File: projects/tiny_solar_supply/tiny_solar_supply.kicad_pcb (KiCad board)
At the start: 2 copper layers, 16 parts, among them J1 Conn_01x02, J2 Conn_01x02, J3 Conn_01x02, J4 Conn_01x02, T1 2N7002 (SOT-23), U1 AP3015AKTR-G1

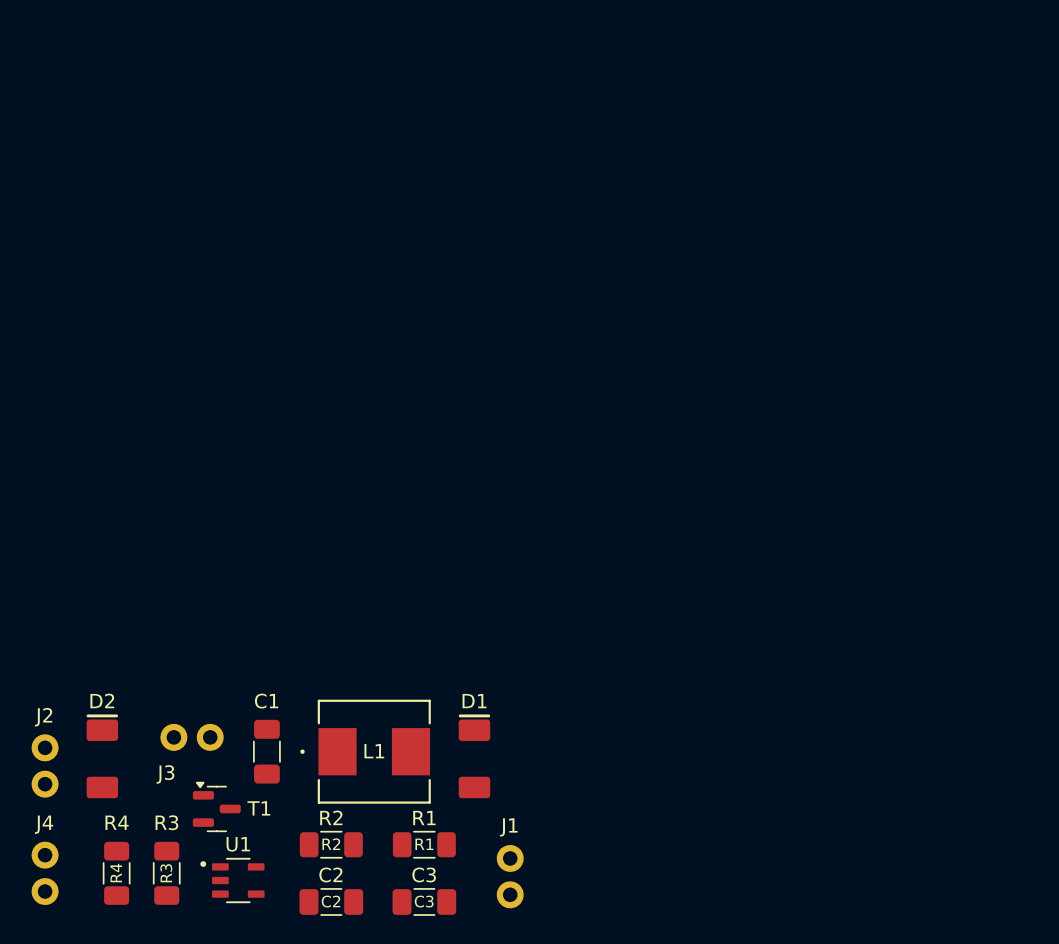
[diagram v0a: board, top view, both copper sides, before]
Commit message: Complete tiny_solar_supply_ v1 PCB layout, add missing 3D models
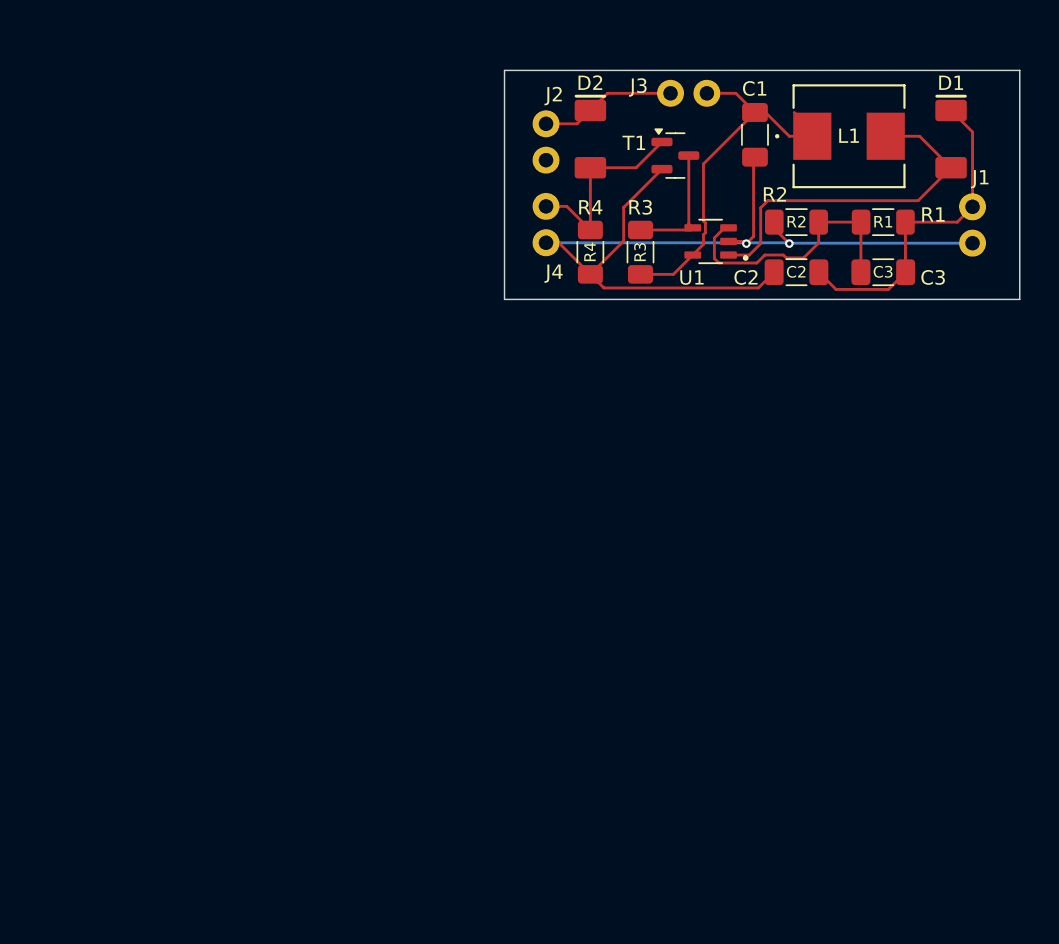
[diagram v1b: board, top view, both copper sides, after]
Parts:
- moved J4 57.3 mm to (133.0, 96.4)
- moved J3 56.8 mm to (141.7, 88.5)
- moved J2 55.9 mm to (133.0, 90.6)
- moved J1 55.8 mm to (162.8, 96.4)
- moved T1 55.8 mm to (142.0, 92.8)
- moved U1 55.5 mm to (144.5, 98.8), turned to 180 degrees
- moved D2 55.1 mm to (136.1, 91.7)
- moved C1 55.0 mm to (147.6, 91.4)
- moved C2 54.7 mm to (150.5, 101.0)
- moved D1 54.6 mm to (161.3, 91.7)
- moved R3 54.6 mm to (139.6, 99.6), turned to -90 degrees
- moved R4 54.6 mm to (136.1, 99.6)
- moved C3 54.4 mm to (156.6, 101.0)
- moved L1 54.3 mm to (154.2, 91.5)
- moved R2 54.3 mm to (150.5, 97.5)
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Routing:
- net GNDD: track 0.00 -> 66.5 mm, vias 0 -> 2
- net Net-(J3-Pin_2): track 0.00 -> 26.5 mm
- net Net-(D1-A): track 0.00 -> 25.0 mm
- net /OUTPUT_POSITIVE: track 0.00 -> 23.0 mm
- net Net-(U1-FB): track 0.00 -> 18.8 mm
- net /SOLAR_POSITIVE: track 0.00 -> 13.9 mm
- net /BATT_POSITIVE: track 0.00 -> 9.58 mm
- net Net-(T1-D): track 0.00 -> 8.88 mm
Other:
- board outline added: 36 x 16 mm

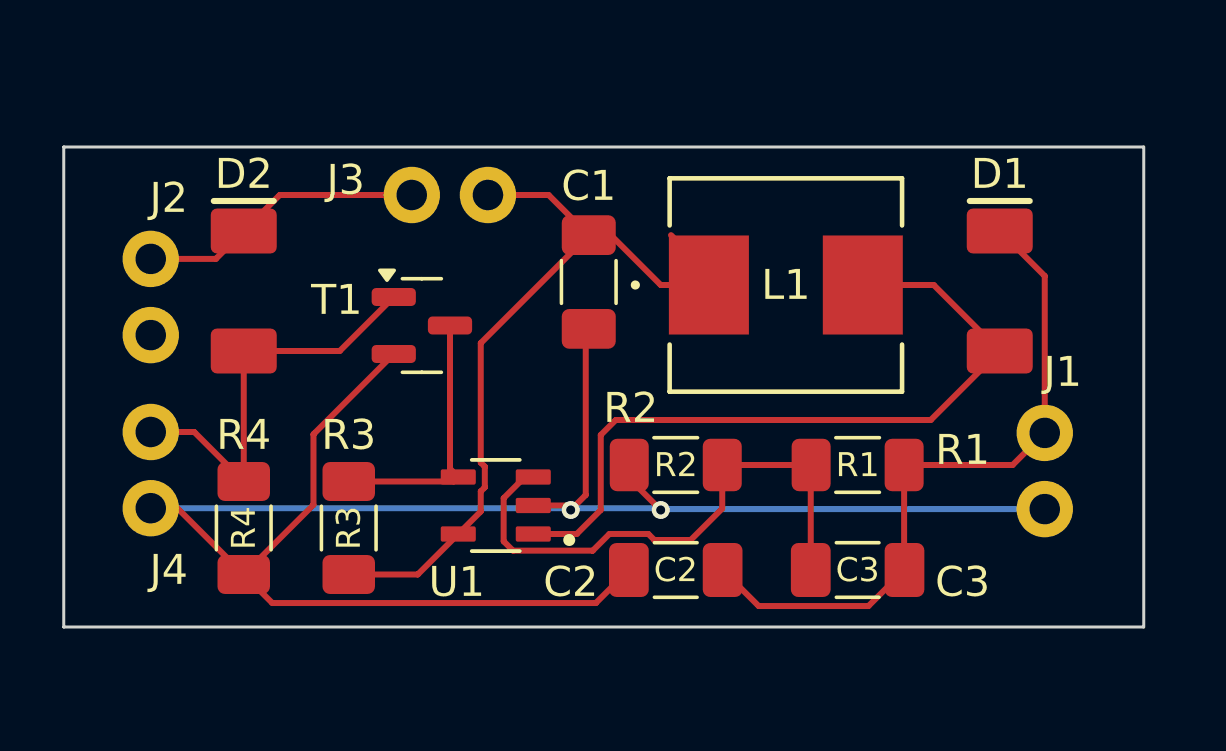
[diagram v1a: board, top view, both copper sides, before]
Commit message: Create v1.0 - first version sent for manufacturing
- in folder versions/ save versions v0.1 and v1.0
- in folder gerbers/ export gerbers of version v1.0
- in folder assets/ rename figures of v0.1 and create figures of v1.0
- update file README.md
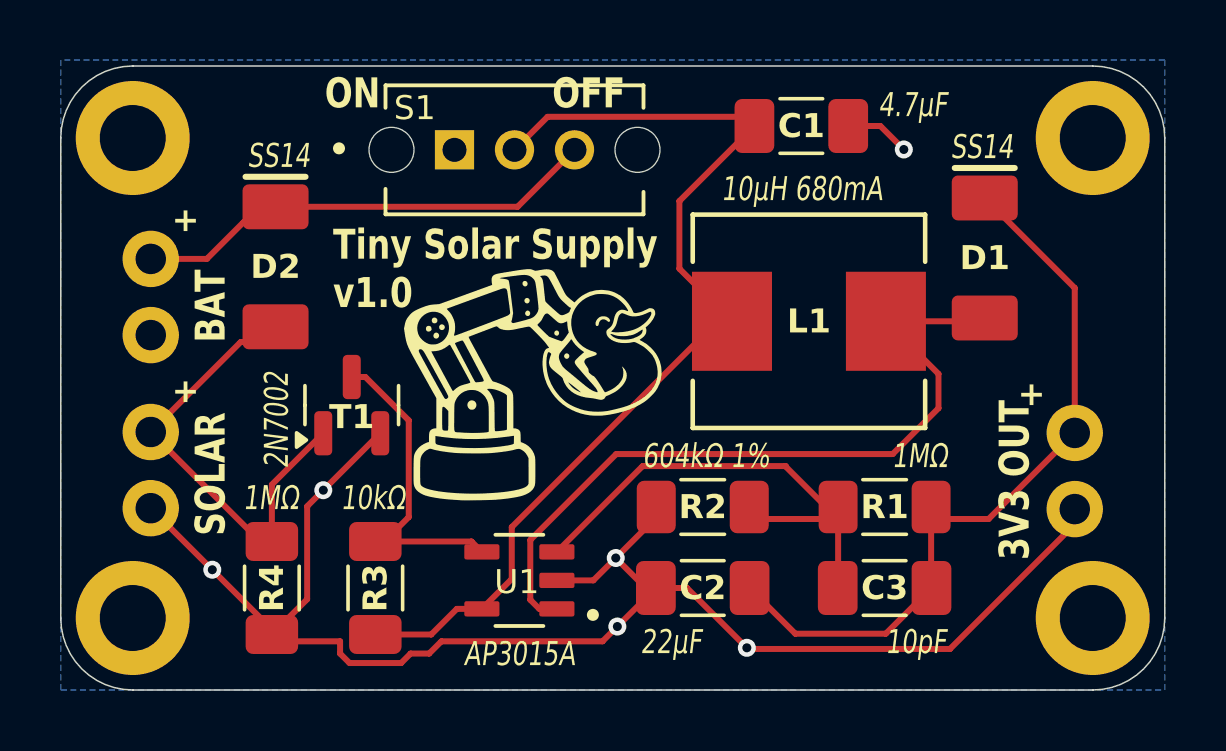
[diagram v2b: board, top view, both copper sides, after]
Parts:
- removed J3: Conn_01x02, SparkFun-Connector:1x02
- added G***: LOGO, MH_logo:robot_duckie_logo_10mm, F.Cu at (145.7, 94.4)
- added REF**: MountingHole_2.2mm_M2_DIN965_Pad, MountingHole:MountingHole_2.2mm_M2_DIN965_Pad, F.Cu at (164.4, 86.6)
- added REF**: MountingHole_2.2mm_M2_DIN965_Pad, MountingHole:MountingHole_2.2mm_M2_DIN965_Pad, F.Cu at (132.4, 102.6)
- added REF**: MountingHole_2.2mm_M2_DIN965_Pad, MountingHole:MountingHole_2.2mm_M2_DIN965_Pad, F.Cu at (164.4, 102.6)
- added REF**: MountingHole_2.2mm_M2_DIN965_Pad, MountingHole:MountingHole_2.2mm_M2_DIN965_Pad, F.Cu at (132.4, 86.6)
- added S1: OS102011MS2QN1, MH_Slide_Switch:SW_OS102011MS2QN1, F.Cu at (145.1, 87.0)
- C1: value 4.7 µF, 50 V, X7R (0805) -> 4.7µF
- C2: value 22 µF, 10 V, X7R (1206) -> 22µF
- C3: value 10 pF, 50 V, X7R (0805) -> 10pF
- D1, D2: value SS14 (DO-214AC) -> SS14
- L1: value 10 µH, 680 mA -> 10µH 680mA
- R1, R4: value 1 MΩ (0805, 0.125 W) -> 1MΩ
- R2: value 604 kΩ, 1% (0805, 0.125 W) -> 604kΩ 1%
- R3: value 10 kΩ (0805, 0.125 W) -> 10kΩ
- T1: value 2N7002 (SOT-23) -> 2N7002
- U1: value AP3015AKTR-G1 -> AP3015A
- moved C1 8.79 mm to (154.7, 86.2), turned to 180 degrees
- moved T1 3.54 mm to (139.7, 95.5), turned to 90 degrees
- moved U1 2.62 mm to (145.3, 101.3)
- moved R4 2.21 mm to (137.0, 101.6)
- moved R3 2.19 mm to (140.5, 101.6)
- moved R1 1.66 mm to (157.5, 98.9)
- moved R2 1.66 mm to (151.4, 98.9)
- moved L1 1.43 mm to (154.9, 92.7)
- moved D2 1.33 mm to (137.2, 90.9)
- moved D1 1.21 mm to (160.8, 90.6)
- moved C2 1.08 mm to (151.4, 101.6)
- moved C3 1.08 mm to (157.5, 101.6)
- moved J1 1.00 mm to (163.8, 96.4)
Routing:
- net GNDD: track 66.5 -> 54.8 mm, vias 2 -> 6
- net Net-(U1-VIN): track 26.5 -> 34.1 mm
- net /BATT_POSITIVE: track 9.58 -> 15.1 mm
- net Net-(T1-D): track 8.88 -> 11.5 mm
- net /OUTPUT_POSITIVE: track 23.0 -> 25.1 mm
- net Net-(U1-FB): track 18.8 -> 17.0 mm
- net /SOLAR_POSITIVE: track 13.9 -> 15.1 mm
- added copper zone on B.Cu, net GNDD
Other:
- board size 36 x 16 mm -> 36.8 x 20.8 mm
- board text added: "+"
- board text added: "ON OFF"
- board text added: "Tiny Solar Supply v1.0"

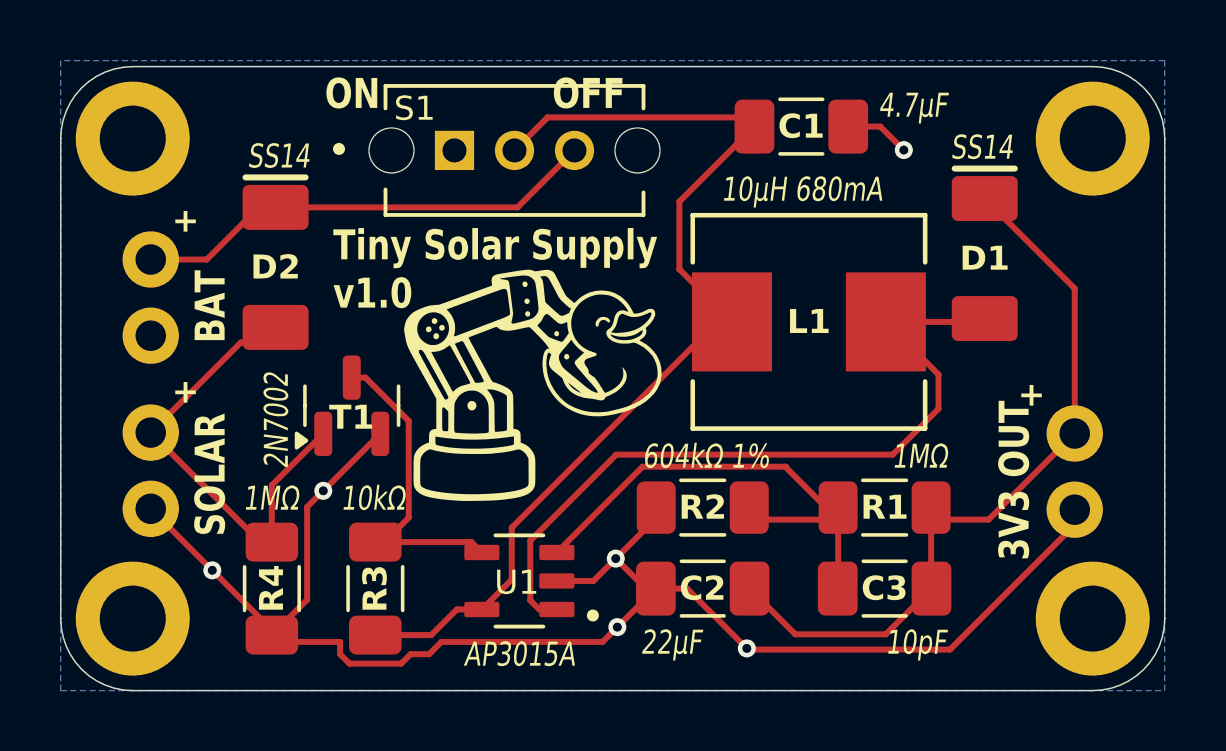
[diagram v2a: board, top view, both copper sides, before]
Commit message: tiny_solar_supply v1.1 initial commit
- improve silkscreen: whit bkg on user labels
- improve routing: vias to GND plane
- add datasheets of AP3015 and L1
- fix switch ON/OFF labels (were reversed)

Pending: Fix wrong L1 footprint.
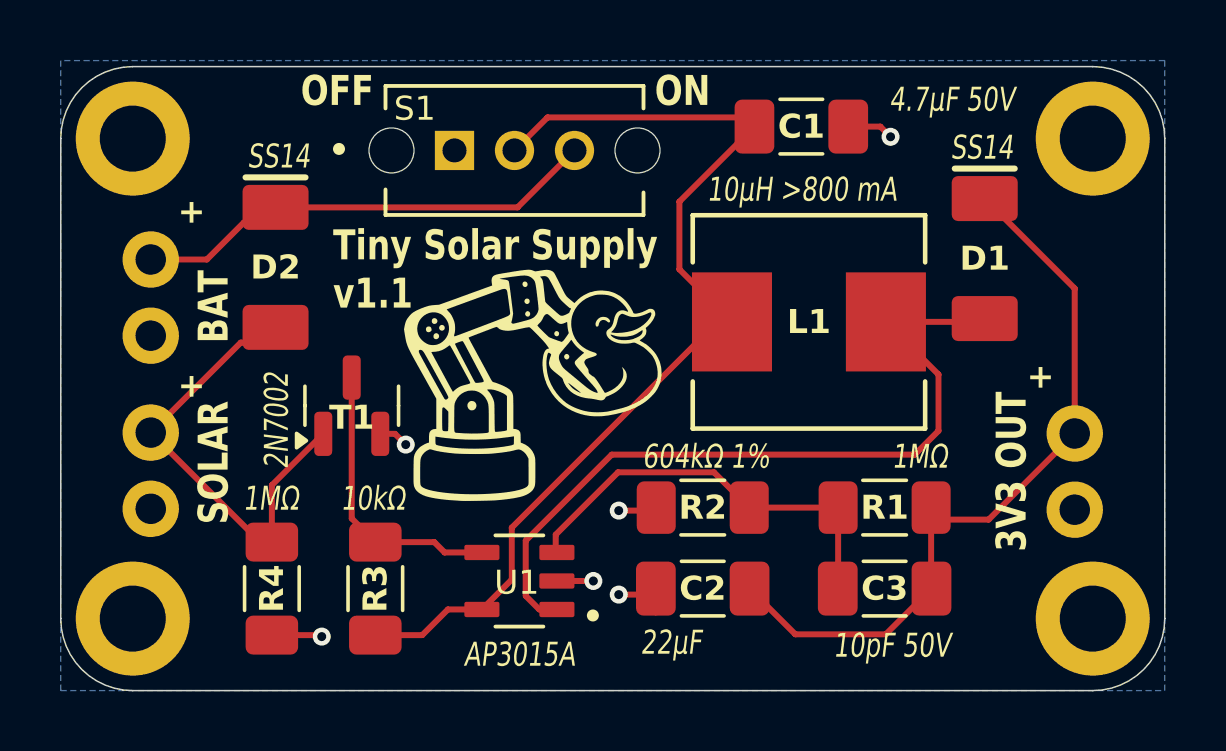
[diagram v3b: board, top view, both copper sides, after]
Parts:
- C1: value 4.7µF -> 4.7µF 50V
- C3: value 10pF -> 10pF 50V
- L1: value 10µH 680mA -> 10µH >800 mA
- R1: value 1MΩ -> 1MΩ
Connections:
- net GNDD renamed GND
- net Net-(D1-A) renamed /SW
- net Net-(T1-D) renamed /~{SHDN}
- net Net-(U1-FB) renamed /FB
- net Net-(U1-VIN) renamed /VIN
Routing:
- net GND: track 54.8 -> 10.5 mm
- net /FB: track 17.0 -> 14.1 mm
- net /~{SHDN}: track 11.5 -> 10.0 mm
- net /SW: track 25.4 -> 26.0 mm
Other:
- board text added: "OFF"
- board text added: "ON"
- board text added: "Tiny Solar Supply v1.1"
- board text removed: "ON OFF"
- board text removed: "Tiny Solar Supply v1.0"
